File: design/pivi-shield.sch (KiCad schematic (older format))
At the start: 1 part

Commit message: Fix #4: add GPIO to reset microcontroller from pi.
* Add a Raspeberry pi pin (GPIO 18) to reset microcontroller.
* Add a Raspebeery pi pin (GPIO 23) to control the microcontroller status.
* Add a RGB LED connected to the microcontroller (PD0, PD1, PD2).
* Rename all the sheets to PIVI v1.1.
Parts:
- added D2: LED_RGB, symbol LED_RGB
- added R1, R2, R3: 4k7, symbol R
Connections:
- net labels added: RESET, control
- wire segments 98 -> 112
- no-connect marks 29 -> 25

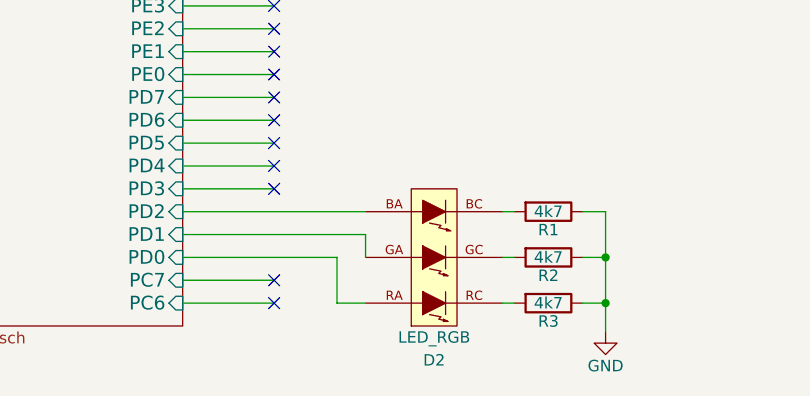
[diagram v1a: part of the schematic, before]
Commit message: Fix #4: Move RGB LED from microcontroller to pi.
* Move RGB LED. Now it is controlled by the raspberry pi.
* Change some new libraries for capacitors and resistors.
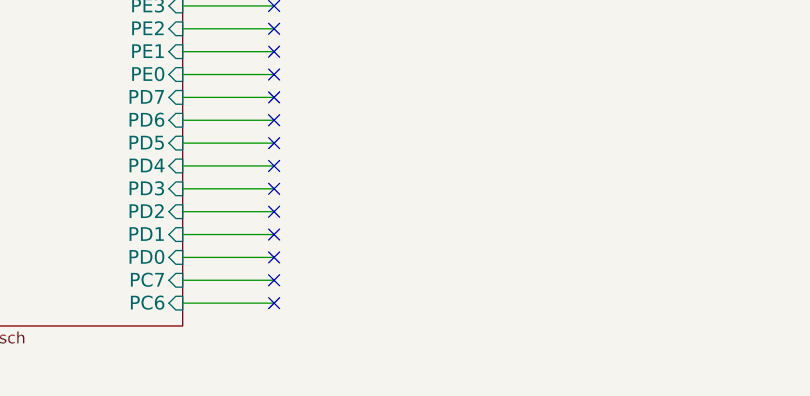
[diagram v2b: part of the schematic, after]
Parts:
- removed D2: LED_RGB, symbol LED_RGB
- removed R1, R2, R3: 4k7, symbol R
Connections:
- wire segments 112 -> 102
- no-connect marks 25 -> 28
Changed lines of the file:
@@
 LIBS:txs0104e
 LIBS:less
-LIBS:pivi-shield-cache
 EELAYER 25 0
 EELAYER END
@@
 Wire Wire Line
 	4675 6925 4275 6925
-Wire Wire Line
-	4275 6825 4950 6825
-Wire Wire Line
-	4275 6725 5075 6725
-Wire Wire Line
-	4275 6625 5075 6625
 NoConn ~ 4675 6525
 Wire Wire Line
@@
 Wire Wire Line
 	2675 6925 2125 6925
-$Comp
-L LED_RGB D2
-U 1 1 558B14D6
-P 5375 6825
-F 0 "D2" H 5375 7275 50  0000 C CNN
-F 1 "LED_RGB" H 5375 7175 50  0000 C CNN
-F 2 "" H 5375 6775 60  0000 C CNN
-F 3 "" H 5375 6775 60  0000 C CNN
-	1    5375 6825
-	-1   0    0    1
-$EndComp
-$Comp
-L R R1
-U 1 1 558B2D23
-P 5875 6625
-F 0 "R1" V 5955 6625 50  0000 C CNN
-F 1 "4k7" V 5875 6625 50  0000 C CNN
-F 2 "" V 5805 6625 30  0000 C CNN
-F 3 "" H 5875 6625 30  0000 C CNN
-	1    5875 6625
-	0    1    1    0
-$EndComp
-$Comp
-L R R2
-U 1 1 558B30B3
-P 5875 6825
-F 0 "R2" V 5955 6825 50  0000 C CNN
-F 1 "4k7" V 5875 6825 50  0000 C CNN
-F 2 "" V 5805 6825 30  0000 C CNN
-F 3 "" H 5875 6825 30  0000 C CNN
-	1    5875 6825
-	0    1    1    0
-$EndComp
-$Comp
-L R R3
-U 1 1 558B31ED
-P 5875 7025
-F 0 "R3" V 5955 7025 50  0000 C CNN
-F 1 "4k7" V 5875 7025 50  0000 C CNN
-F 2 "" V 5805 7025 30  0000 C CNN
-F 3 "" H 5875 7025 30  0000 C CNN
-	1    5875 7025
-	0    1    1    0
-$EndComp
-Wire Wire Line
-	6025 6625 6125 6625
-Wire Wire Line
-	6125 6625 6125 7150
-Wire Wire Line
-	6025 6825 6125 6825
-Connection ~ 6125 6825
-Wire Wire Line
-	6025 7025 6125 7025
-Connection ~ 6125 7025
-Wire Wire Line
-	5675 7025 5725 7025
-Wire Wire Line
-	5725 6825 5675 6825
-Wire Wire Line
-	5675 6625 5725 6625
-$Comp
-L GND #PWR09
-U 1 1 558B3E85
-P 6125 7150
-F 0 "#PWR09" H 6125 6900 50  0001 C CNN
-F 1 "GND" H 6125 7000 50  0000 C CNN
-F 2 "" H 6125 7150 60  0000 C CNN
-F 3 "" H 6125 7150 60  0000 C CNN
-	1    6125 7150
-	1    0    0    -1
-$EndComp
-Wire Wire Line
-	4950 6825 4950 7025
-Wire Wire Line
-	4950 7025 5075 7025
-Wire Wire Line
-	5075 6725 5075 6825
+NoConn ~ 4675 6825
+Wire Wire Line
+	4675 6825 4275 6825
+NoConn ~ 4675 6725
+Wire Wire Line
+	4675 6725 4275 6725
+NoConn ~ 4675 6625
+Wire Wire Line
+	4675 6625 4275 6625
 $EndSCHEMATC

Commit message: Changing footprints of  audio jack3.5mm Added new footprints. Added debub uart,  reference voltage Added two extra circuits for voltage measure Moving to PIVI 2.0, added circuits for current clamps
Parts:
- added R1: 2.222K, symbol R
- added R2: 10K, symbol R
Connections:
- net labels added: CT1_1, CT1_2, CT1_Detector, CT2_1, CT2_2, CT2_Detector, CT3_1, CT3_2, CT3_Detector, CT4_1, CT4_2, CT4_Detector, CT5_1, CT5_2, CT5_Detector, CT6_1, CT6_2, CT6_Detector, Control, Current_AD_1, Current_AD_2, Current_AD_3, Current_AD_4, Current_AD_5, Current_AD_6, Neutral_Filtered, Neutral_Line, Phase_Line, V_REF, Voltage_AD_1, Voltage_AD_2, Voltage_AD_3
- net labels removed: Current1_AD, Current2_AD, Current3_AD, Current4_AD, Current5_AD, Current6_AD, Neutral, Neutral1_In, Neutral1_Out, Phase1_In, Phase1_Out, Phase2_In, Phase2_Out, Phase3_In, Phase3_Out, Phase4_In, Phase4_Out, Phase5_In, Phase5_Out, Phase6_In, Phase6_Out, Voltage1_AD1, Voltage2_AD1, Voltage3_AD1, Voltage4_AD1, Voltage5_AD1, Voltage6_AD1, control
- wire segments 102 -> 108
- no-connect marks 28 -> 23
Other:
- note added: "2.7 V"
- note added: "Voltage Reference\n"
- note added: "Voltage Regulator"
- moved on the sheet: L1

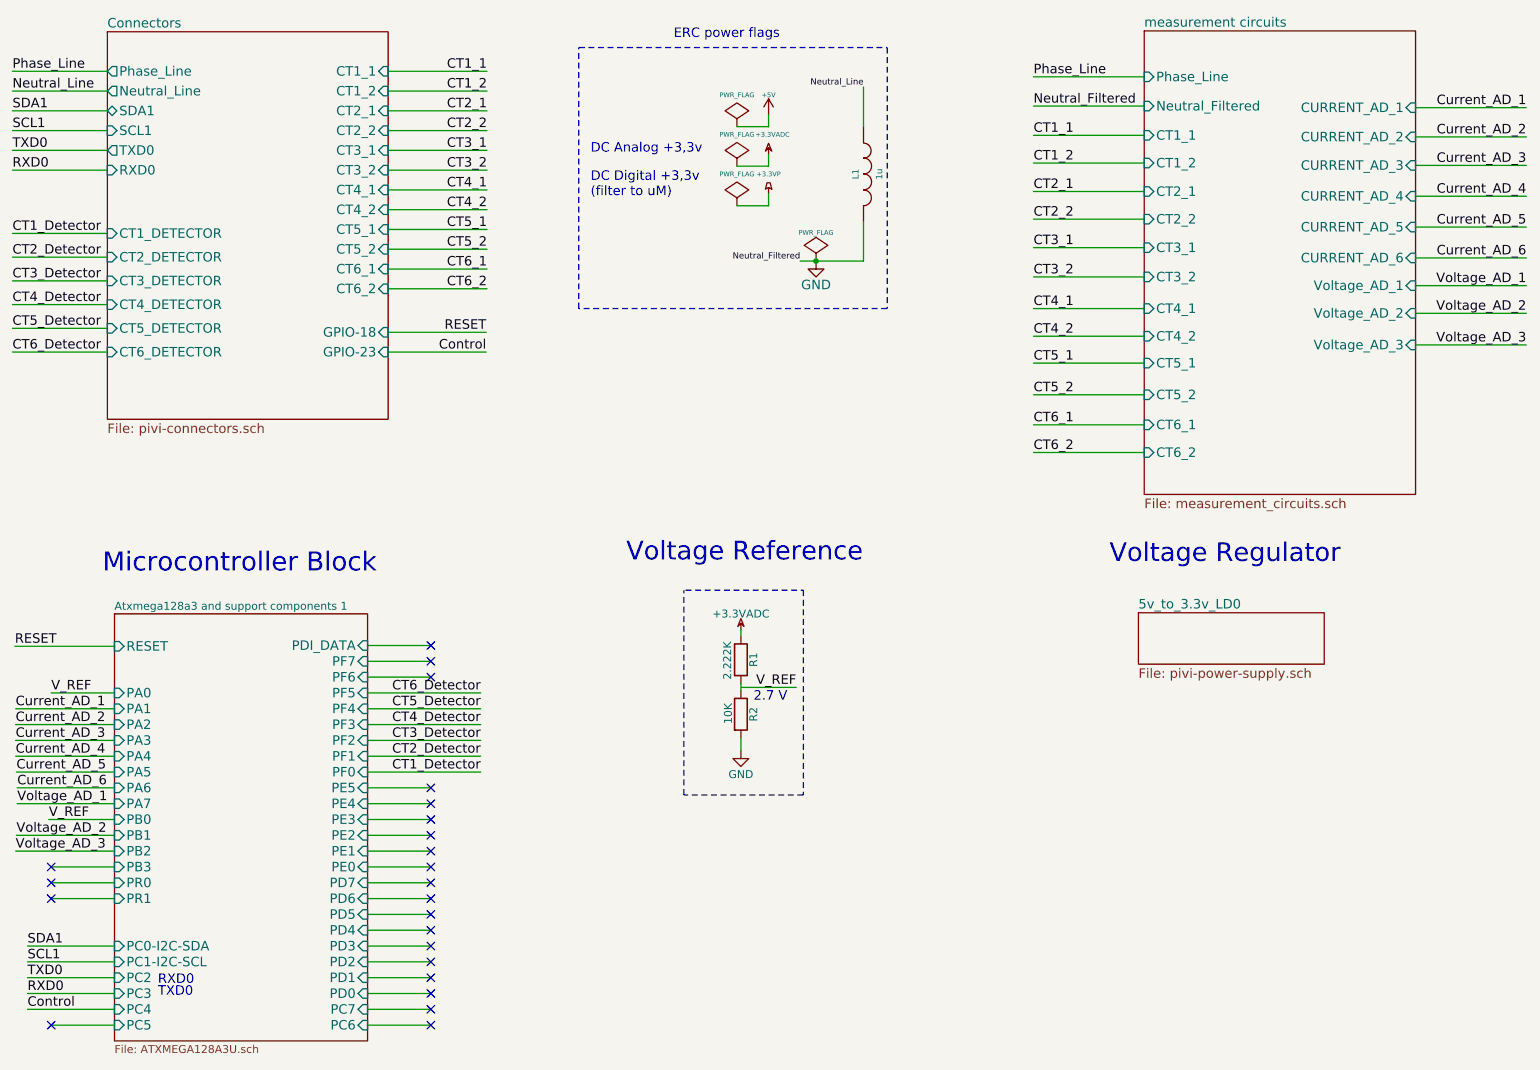
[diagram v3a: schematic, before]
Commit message: Fix connection problems.
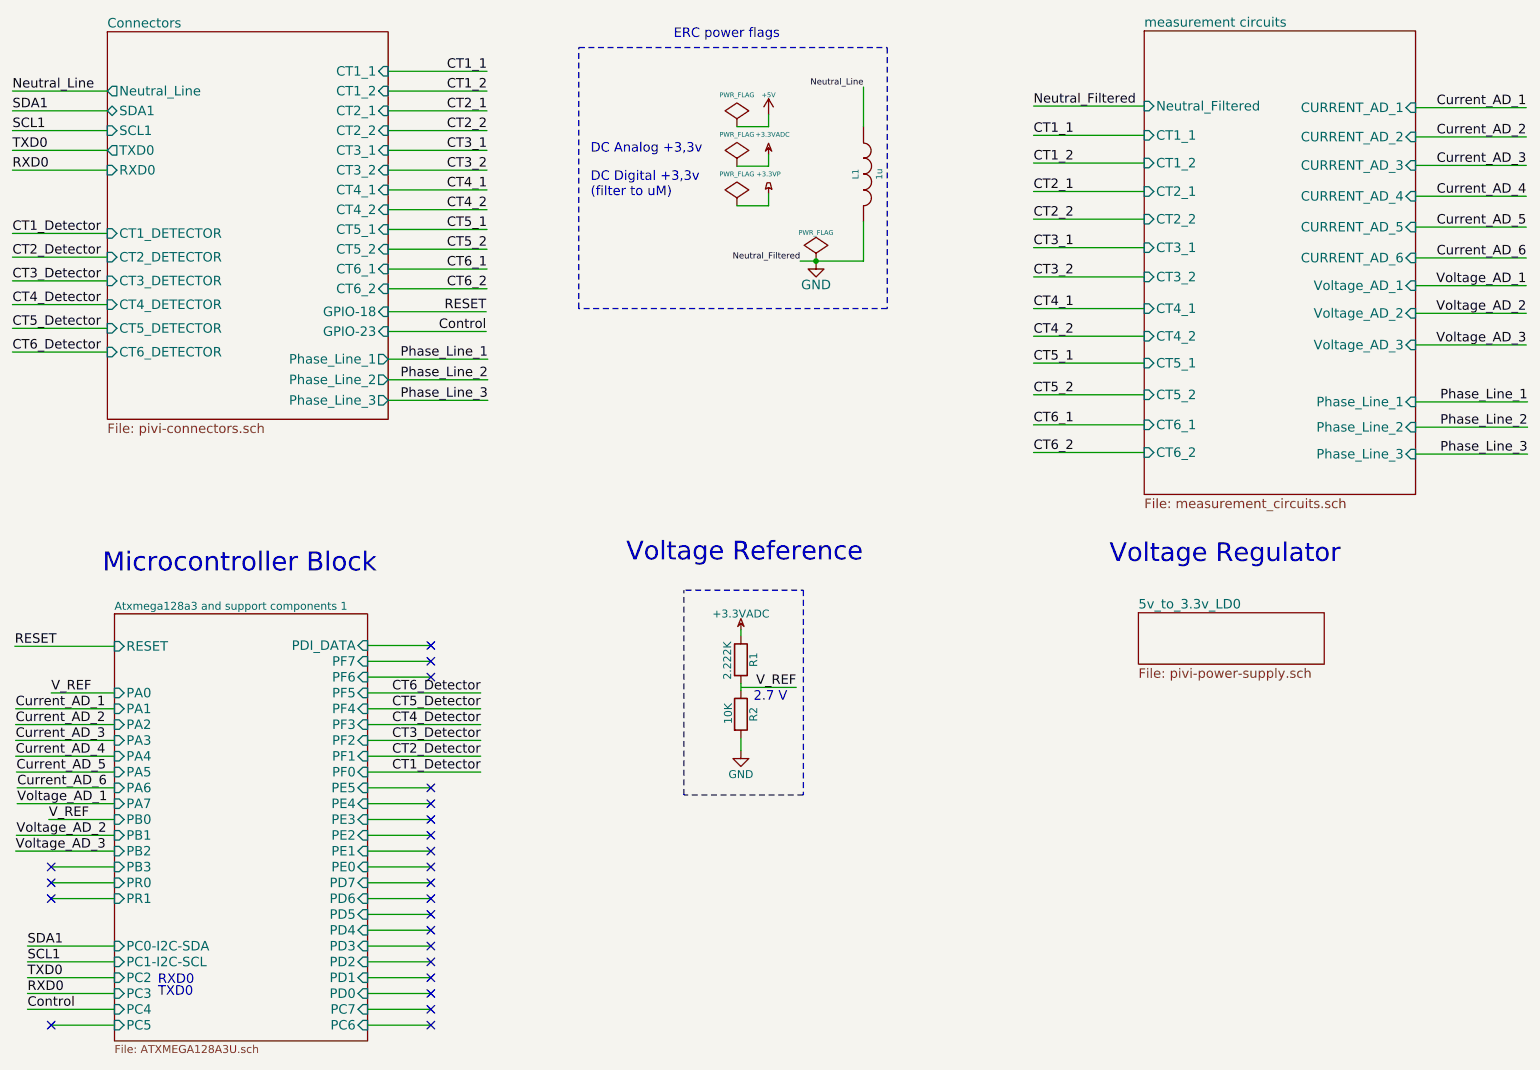
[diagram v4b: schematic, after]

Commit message: Starting PIVI 2.0 * sch ready. * components in PCB placed.
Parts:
- R1, R2: footprint (none) -> Resistors_SMD:R_0603
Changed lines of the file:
@@
 Current_AD_6
 $Comp
-L +5V #PWR3
+L +5V #PWR01
 U 1 1 54928783
 P 5855 1475
-F 0 "#PWR3" H 5855 1565 20  0001 C CNN
+F 0 "#PWR01" H 5855 1565 20  0001 C CNN
 F 1 "+5V" H 5855 1600 30  0000 C CNN
 F 2 "" H 5855 1475 60  0000 C CNN
@@
 $EndComp
 $Comp
-L PWR_FLAG #FLG1
+L PWR_FLAG #FLG02
 U 1 1 54928C31
 P 5655 1550
-F 0 "#FLG1" H 5655 1645 30  0001 C CNN
+F 0 "#FLG02" H 5655 1645 30  0001 C CNN
 F 1 "PWR_FLAG" H 5655 1750 30  0000 C CNN
 F 2 "" H 5655 1550 60  0000 C CNN
@@
 $EndSheet
 $Comp
-L PWR_FLAG #FLG2
+L PWR_FLAG #FLG03
 U 1 1 548F827F
 P 5655 1800
-F 0 "#FLG2" H 5655 1895 30  0001 C CNN
+F 0 "#FLG03" H 5655 1895 30  0001 C CNN
 F 1 "PWR_FLAG" H 5655 2000 30  0000 C CNN
 F 2 "" H 5655 1800 60  0000 C CNN
@@
 $EndComp
 $Comp
-L PWR_FLAG #FLG3
+L PWR_FLAG #FLG04
 U 1 1 548F891D
 P 5655 2050
-F 0 "#FLG3" H 5655 2145 30  0001 C CNN
+F 0 "#FLG04" H 5655 2145 30  0001 C CNN
 F 1 "PWR_FLAG" H 5655 2250 30  0000 C CNN
 F 2 "" H 5655 2050 60  0000 C CNN
@@
 $EndComp
 $Comp
-L +3.3VADC #PWR4
+L +3.3VADC #PWR05
 U 1 1 548F9301
 P 5855 1725
-F 0 "#PWR4" H 5855 1845 20  0001 C CNN
+F 0 "#PWR05" H 5855 1845 20  0001 C CNN
 F 1 "+3.3VADC" H 5880 1850 30  0000 C CNN
 F 2 "" H 5855 1725 60  0000 C CNN
@@
 $EndComp
 $Comp
-L +3.3VP #PWR5
+L +3.3VP #PWR06
 U 1 1 548F9315
 P 5855 1975
-F 0 "#PWR5" H 5905 2005 20  0001 C CNN
+F 0 "#PWR06" H 5905 2005 20  0001 C CNN
 F 1 "+3.3VP" H 5855 2100 30  0000 C CNN
 F 2 "" H 5855 1975 60  0000 C CNN
@@
 TXD0
 $Comp
-L PWR_FLAG #FLG4
+L PWR_FLAG #FLG07
 U 1 1 5491BF45
 P 6155 2400
-F 0 "#FLG4" H 6155 2495 30  0001 C CNN
+F 0 "#FLG07" H 6155 2495 30  0001 C CNN
 F 1 "PWR_FLAG" H 6155 2580 30  0000 C CNN
 F 2 "" H 6155 2400 60  0000 C CNN
@@
 $EndComp
 $Comp
-L GND #PWR6
+L GND #PWR08
 U 1 1 54BFB838
 P 6155 2400
-F 0 "#PWR6" H 6155 2150 60  0001 C CNN
+F 0 "#PWR08" H 6155 2150 60  0001 C CNN
 F 1 "GND" H 6155 2250 60  0000 C CNN
 F 2 "" H 6155 2400 60  0000 C CNN
@@
 Current_AD_1
 $Comp
-L +3.3VADC #PWR1
+L +3.3VADC #PWR09
 U 1 1 55BC3462
 P 5680 4730
-F 0 "#PWR1" H 5830 4680 50  0001 C CNN
+F 0 "#PWR09" H 5830 4680 50  0001 C CNN
 F 1 "+3.3VADC" H 5680 4830 50  0000 C CNN
 F 2 "" H 5680 4730 60  0000 C CNN
@@
 F 0 "R1" V 5760 4920 50  0000 C CNN
 F 1 "2.222K" V 5595 4915 50  0000 C CNN
-F 2 "" V 5610 4920 30  0000 C CNN
+F 2 "Resistors_SMD:R_0603" V 5610 4920 30  0001 C CNN
 F 3 "" H 5680 4920 30  0000 C CNN
 	1    5680 4920
@@
 F 0 "R2" V 5760 5265 50  0000 C CNN
 F 1 "10K" V 5600 5270 50  0000 C CNN
-F 2 "" V 5610 5265 30  0000 C CNN
+F 2 "Resistors_SMD:R_0603" V 5610 5265 30  0001 C CNN
 F 3 "" H 5680 5265 30  0000 C CNN
 	1    5680 5265
@@
 $EndComp
 $Comp
-L GND #PWR2
+L GND #PWR010
 U 1 1 55BC74D1
 P 5680 5495
-F 0 "#PWR2" H 5680 5245 50  0001 C CNN
+F 0 "#PWR010" H 5680 5245 50  0001 C CNN
 F 1 "GND" H 5680 5345 50  0000 C CNN
 F 2 "" H 5680 5495 60  0000 C CNN
